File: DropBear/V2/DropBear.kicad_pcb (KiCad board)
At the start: 2 copper layers, 116.1 x 98 mm, 201 parts, among them IC1 MAX9926UAEE_V+, IC2 ZXMS6006DT8, IC3 ZXMS6006DT8, IC4 ZXMS6006DT8, IC5 ZXMS6006DT8, J1 Delphi_Sicma_24, J2 Delphi_Sicma_24, J3 EBC05DRXN, Q2 Q_DUAL_NMOS_S1G1D2S2G2D1, Q3 Q_DUAL_NMOS_S1G1D2S2G2D1, SW1 SW_DPDT_x2, SW2 SW_DPDT_x2, SW3 SW_DIP_x02, SW4 SW_DPDT_x2, SW5 SW_DPDT_x2, U1 Teensy4.1, U10 TC4424A, U11 KP234, U12 LMV324LIDT, U13 SP720, U14 LMV324LIDT, U15 MC78M05_TO252, U2 MCP2562-E-SN, U3 W25Q32JVSS, U5 TC4424A, U6 TC4424A, U7 MC33810, U8 MC33810, U9 TC4424A

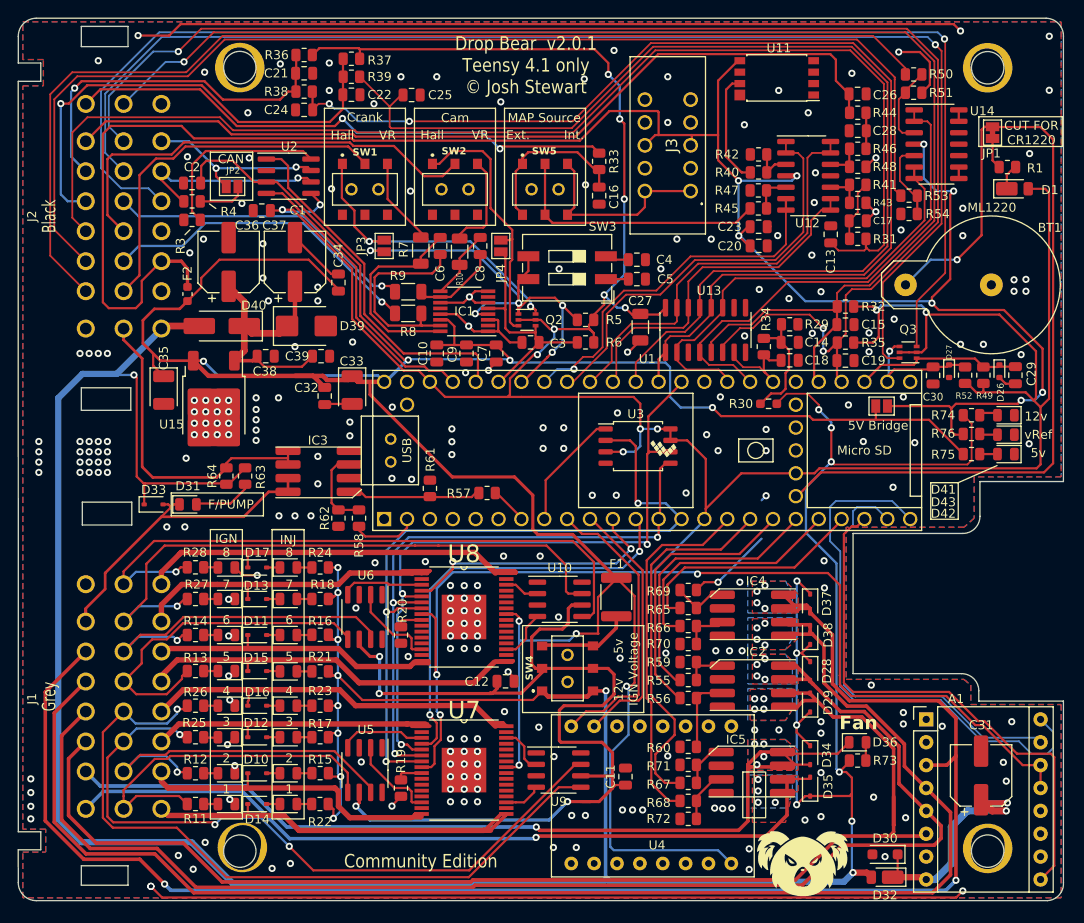
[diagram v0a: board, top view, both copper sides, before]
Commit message: Dropbear v2.0.2 minor update
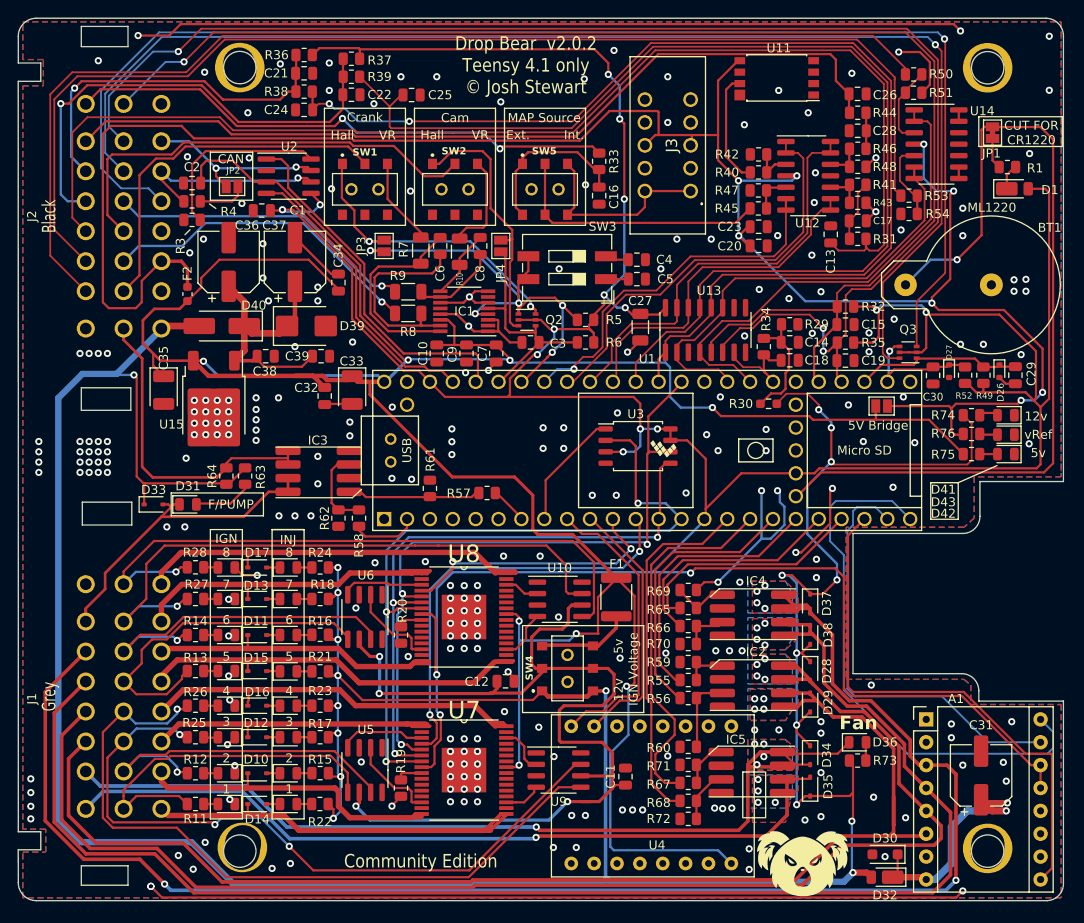
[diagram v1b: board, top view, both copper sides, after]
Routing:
- net GND: track 253.3 -> 274.4 mm, vias 262 -> 265
- net 12V-SW: track 406.3 -> 391.0 mm
- net SPARE1-OUT: track 178.0 -> 171.6 mm
- net +3V3: track 427.4 -> 428.6 mm
- net MCU-D28: track 27.0 -> 25.9 mm
- net MCU-D30: track 60.5 -> 59.5 mm
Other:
- board text added: "Drop Bear v2.0.2 Teensy 4.1 only © Josh Stewart"
- board text removed: "Drop Bear v2.0.1 Teensy 4.1 only © Josh Stewart"
